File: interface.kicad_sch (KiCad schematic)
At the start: 8 parts, among them J5 Conn_01x16

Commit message: PN update
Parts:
- FB2: PN (none) -> BLM18KG601SH1D
- J5: value Conn_01x16 -> DA15_CONN; PN (none) -> TSM-108-01-L-DV-P-TR
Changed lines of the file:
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@@
       (effects (font (size 1.27 1.27)))
     )
-    (property "Value" "Conn_01x16" (at 109.22 120.1999 0)
+    (property "Value" "DA15_CONN" (at 109.22 120.1999 0)
       (effects (font (size 1.27 1.27)))
     )
@@
     )
     (property "Datasheet" "~" (at 109.22 140.97 0)
+      (effects (font (size 1.27 1.27)) hide)
+    )
+    (property "PN" "TSM-108-01-L-DV-P-TR" (at 109.22 140.97 0)
       (effects (font (size 1.27 1.27)) hide)
     )
@@
       (effects (font (size 1.27 1.27)) hide)
     )
-    (property "PN" "" (at 278.13 128.27 90)
-      (effects (font (size 1.27 1.27)) hide)
-    )
+    (property "PN" "BLM18KG601SH1D" (at 278.13 128.27 90)
+      (effects (font (size 1.27 1.27)) hide)
+    )

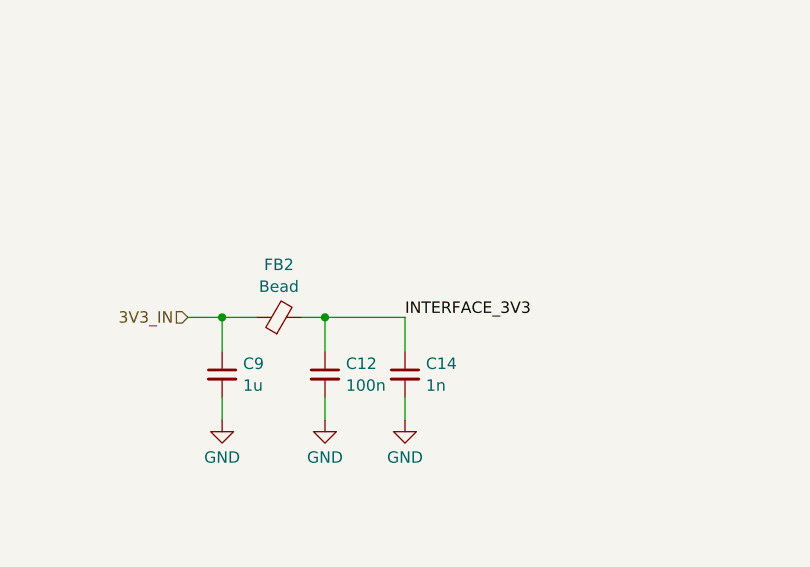
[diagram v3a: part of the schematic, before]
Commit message: `PWR_FLAG`, ERC cleanup
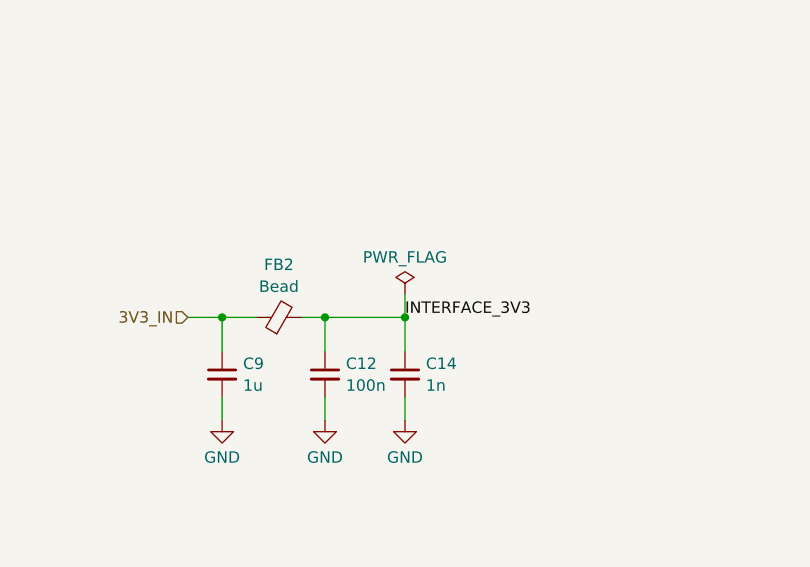
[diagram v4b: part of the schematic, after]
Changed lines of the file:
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@@
     (comment 1 "Wojciech Kaczmarski, SP5WWP")
+  )
+  (junction (at 292.1 128.27) (diameter 0) (color 0 0 0 0)
   )
   (junction (at 119.38 161.29) (diameter 0) (color 0 0 0 0)
@@
   )
   (wire (pts (xy 114.3 156.21) (xy 146.05 156.21))
+    (stroke (width 0) (type default))
+  )
+  (wire (pts (xy 292.1 125.73) (xy 292.1 128.27))
     (stroke (width 0) (type default))
   )
@@
         )
       )
+    )
+  )
+  (symbol (lib_id "power:PWR_FLAG") (at 292.1 125.73 0) (unit 1)
+    (in_bom yes) (on_board yes) (dnp no) (fields_autoplaced)
+    (property "Reference" "#FLG01" (at 292.1 123.825 0)
+      (effects (font (size 1.27 1.27)) hide)
+    )
+    (property "Value" "PWR_FLAG" (at 292.1 121.5969 0)
+      (effects (font (size 1.27 1.27)))
+    )
+    (property "Footprint" "" (at 292.1 125.73 0)
+      (effects (font (size 1.27 1.27)) hide)
+    )
+    (property "Datasheet" "~" (at 292.1 125.73 0)
+      (effects (font (size 1.27 1.27)) hide)
+    )
+    (pin "1")
+    (instances
+      (project "m17-rru-rf"
+        (path "/4c42207c-9e6b-42da-ad38-da126b892014/270fa747-1697-46c9-b996-5c9733c883e2"
+          (reference "#FLG01") (unit 1)
+        )
+        (path "/4c42207c-9e6b-42da-ad38-da126b892014/3ea647a3-6e2c-4a7a-bdb8-a6b94119ef02"
+          (reference "#FLG05") (unit 1)
+        )
+      )

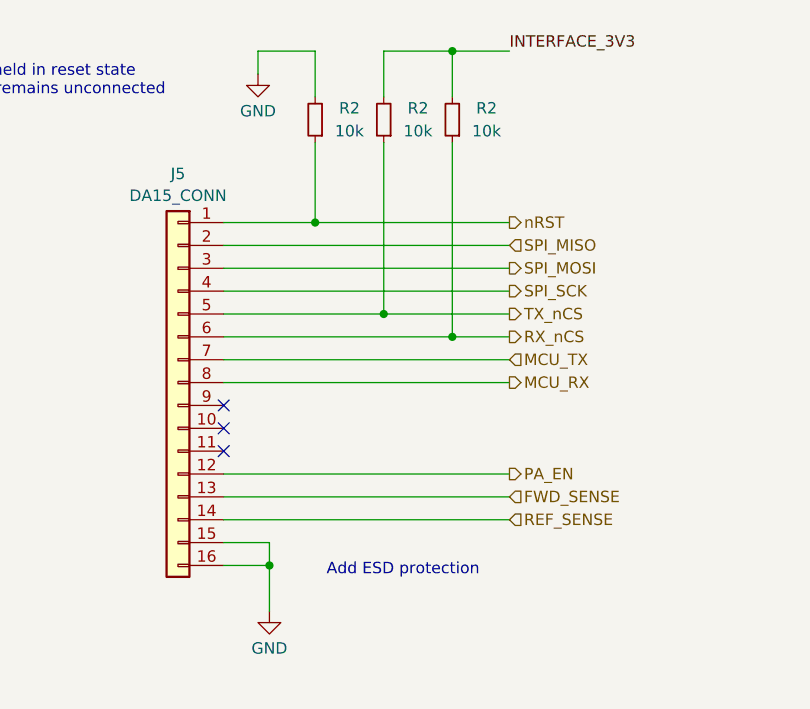
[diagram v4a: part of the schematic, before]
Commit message: TP updates, temp sensor added
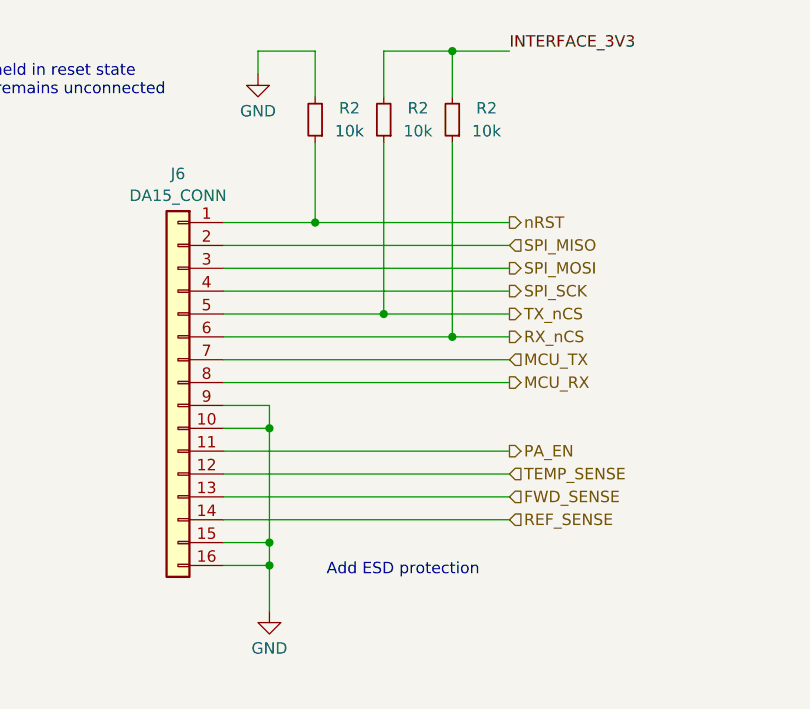
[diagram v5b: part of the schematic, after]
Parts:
- renumbered J5 to J6
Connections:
- net GND: now also J6.10 (Pin_10), J6.9 (Pin_9)
- net PA_EN: now also J6.11 (Pin_11); no longer J6.12 (Pin_12)
- new net TEMP_SENSE: J6.12 (Pin_12)
- no-connect marks 3 -> 0
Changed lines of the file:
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@@
     (comment 1 "Wojciech Kaczmarski, SP5WWP")
   )
+  (junction (at 119.38 158.75) (diameter 0) (color 0 0 0 0)
+  )
   (junction (at 292.1 128.27) (diameter 0) (color 0 0 0 0)
   )
@@
   (junction (at 139.7 135.89) (diameter 0) (color 0 0 0 0)
   )
+  (junction (at 119.38 146.05) (diameter 0) (color 0 0 0 0)
+  )
   (junction (at 283.21 128.27) (diameter 0) (color 0 0 0 0)
   )
@@
   (junction (at 271.78 128.27) (diameter 0) (color 0 0 0 0)
   )
-  (no_connect (at 114.3 143.51))
-  (no_connect (at 114.3 146.05))
-  (no_connect (at 114.3 148.59))
   (wire (pts (xy 124.46 114.3) (xy 124.46 123.19))
     (stroke (width 0) (type default))
   )
+  (wire (pts (xy 114.3 148.59) (xy 146.05 148.59))
+    (stroke (width 0) (type default))
+  )
+  (wire (pts (xy 114.3 125.73) (xy 146.05 125.73))
+    (stroke (width 0) (type default))
+  )
+  (wire (pts (xy 118.11 106.68) (xy 118.11 104.14))
+    (stroke (width 0) (type default))
+  )
+  (wire (pts (xy 132.08 133.35) (xy 146.05 133.35))
+    (stroke (width 0) (type default))
+  )
+  (wire (pts (xy 283.21 137.16) (xy 283.21 139.7))
+    (stroke (width 0) (type default))
+  )
+  (wire (pts (xy 119.38 158.75) (xy 119.38 161.29))
+    (stroke (width 0) (type default))
+  )
+  (wire (pts (xy 292.1 137.16) (xy 292.1 139.7))
+    (stroke (width 0) (type default))
+  )
+  (wire (pts (xy 292.1 132.08) (xy 292.1 128.27))
+    (stroke (width 0) (type default))
+  )
+  (wire (pts (xy 132.08 114.3) (xy 132.08 133.35))
+    (stroke (width 0) (type default))
+  )
   (wire (pts (xy 114.3 151.13) (xy 146.05 151.13))
     (stroke (width 0) (type default))
   )
-  (wire (pts (xy 114.3 125.73) (xy 146.05 125.73))
-    (stroke (width 0) (type default))
-  )
-  (wire (pts (xy 118.11 106.68) (xy 118.11 104.14))
-    (stroke (width 0) (type default))
-  )
-  (wire (pts (xy 132.08 133.35) (xy 146.05 133.35))
-    (stroke (width 0) (type default))
-  )
-  (wire (pts (xy 283.21 137.16) (xy 283.21 139.7))
-    (stroke (width 0) (type default))
-  )
-  (wire (pts (xy 119.38 158.75) (xy 119.38 161.29))
-    (stroke (width 0) (type default))
-  )
-  (wire (pts (xy 292.1 137.16) (xy 292.1 139.7))
-    (stroke (width 0) (type default))
-  )
-  (wire (pts (xy 292.1 132.08) (xy 292.1 128.27))
-    (stroke (width 0) (type default))
-  )
-  (wire (pts (xy 132.08 114.3) (xy 132.08 133.35))
-    (stroke (width 0) (type default))
-  )
   (wire (pts (xy 114.3 156.21) (xy 146.05 156.21))
     (stroke (width 0) (type default))
@@
     (stroke (width 0) (type default))
   )
+  (wire (pts (xy 114.3 146.05) (xy 119.38 146.05))
+    (stroke (width 0) (type default))
+  )
   (wire (pts (xy 119.38 161.29) (xy 119.38 166.37))
     (stroke (width 0) (type default))
@@
     (stroke (width 0) (type default))
   )
+  (wire (pts (xy 114.3 143.51) (xy 119.38 143.51))
+    (stroke (width 0) (type default))
+  )
   (wire (pts (xy 132.08 104.14) (xy 139.7 104.14))
     (stroke (width 0) (type default))
   )
+  (wire (pts (xy 119.38 143.51) (xy 119.38 146.05))
+    (stroke (width 0) (type default))
+  )
   (wire (pts (xy 132.08 109.22) (xy 132.08 104.14))
     (stroke (width 0) (type default))
@@
   )
   (wire (pts (xy 139.7 135.89) (xy 146.05 135.89))
+    (stroke (width 0) (type default))
+  )
+  (wire (pts (xy 119.38 146.05) (xy 119.38 158.75))
     (stroke (width 0) (type default))
   )
@@
     (effects (font (size 1.27 1.27)) (justify left bottom))
   )
+  (hierarchical_label "TEMP_SENSE" (shape input) (at 146.05 151.13 0) (fields_autoplaced)
+    (effects (font (size 1.27 1.27)) (justify left))
+  )
   (hierarchical_label "FWD_SENSE" (shape input) (at 146.05 153.67 0) (fields_autoplaced)
     (effects (font (size 1.27 1.27)) (justify left))
@@
     (effects (font (size 1.27 1.27)) (justify left))
   )
-  (hierarchical_label "PA_EN" (shape output) (at 146.05 151.13 0) (fields_autoplaced)
+  (hierarchical_label "PA_EN" (shape output) (at 146.05 148.59 0) (fields_autoplaced)
     (effects (font (size 1.27 1.27)) (justify left))
   )
@@
   (symbol (lib_id "Connector_Generic:Conn_01x16") (at 109.22 140.97 0) (mirror y) (unit 1)
     (in_bom yes) (on_board yes) (dnp no) (fields_autoplaced)
-    (property "Reference" "J5" (at 109.22 117.7757 0)
+    (property "Reference" "J6" (at 109.22 117.7757 0)
       (effects (font (size 1.27 1.27)))
     )
@@
       (project "m17-rru-rf"
         (path "/4c42207c-9e6b-42da-ad38-da126b892014/3ea647a3-6e2c-4a7a-bdb8-a6b94119ef02"
-          (reference "J5") (unit 1)
+          (reference "J6") (unit 1)
         )
       )
@@
         )
         (path "/4c42207c-9e6b-42da-ad38-da126b892014/3ea647a3-6e2c-4a7a-bdb8-a6b94119ef02"
-          (reference "#PWR0110") (unit 1)
+          (reference "#PWR0115") (unit 1)
         )
       )
@@
         )
         (path "/4c42207c-9e6b-42da-ad38-da126b892014/3ea647a3-6e2c-4a7a-bdb8-a6b94119ef02"
-          (reference "#PWR0112") (unit 1)
+          (reference "#PWR0117") (unit 1)
         )
       )
@@
         )
         (path "/4c42207c-9e6b-42da-ad38-da126b892014/3ea647a3-6e2c-4a7a-bdb8-a6b94119ef02"
-          (reference "#PWR0111") (unit 1)
+          (reference "#PWR0116") (unit 1)
         )
       )
@@
         )
         (path "/4c42207c-9e6b-42da-ad38-da126b892014/3ea647a3-6e2c-4a7a-bdb8-a6b94119ef02"
-          (reference "C89") (unit 1)
+          (reference "C92") (unit 1)
         )
       )
@@
         )
         (path "/4c42207c-9e6b-42da-ad38-da126b892014/3ea647a3-6e2c-4a7a-bdb8-a6b94119ef02"
-          (reference "C87") (unit 1)
+          (reference "C90") (unit 1)
         )
       )
@@
         )
         (path "/4c42207c-9e6b-42da-ad38-da126b892014/3ea647a3-6e2c-4a7a-bdb8-a6b94119ef02"
-          (reference "FB7") (unit 1)
+          (reference "FB9") (unit 1)
         )
       )
@@
         )
         (path "/4c42207c-9e6b-42da-ad38-da126b892014/3ea647a3-6e2c-4a7a-bdb8-a6b94119ef02"
-          (reference "C88") (unit 1)
+          (reference "C91") (unit 1)
         )
       )
@@
         )
         (path "/4c42207c-9e6b-42da-ad38-da126b892014/3ea647a3-6e2c-4a7a-bdb8-a6b94119ef02"
-          (reference "#PWR0114") (unit 1)
+          (reference "#PWR0119") (unit 1)
         )
       )
@@
         )
         (path "/4c42207c-9e6b-42da-ad38-da126b892014/3ea647a3-6e2c-4a7a-bdb8-a6b94119ef02"
-          (reference "#FLG05") (unit 1)
+          (reference "#FLG08") (unit 1)
         )
       )
@@
         )
         (path "/4c42207c-9e6b-42da-ad38-da126b892014/3ea647a3-6e2c-4a7a-bdb8-a6b94119ef02"
-          (reference "#PWR0113") (unit 1)
-        )
-      )
+          (reference "#PWR0118") (unit 1)
+        )
+      )

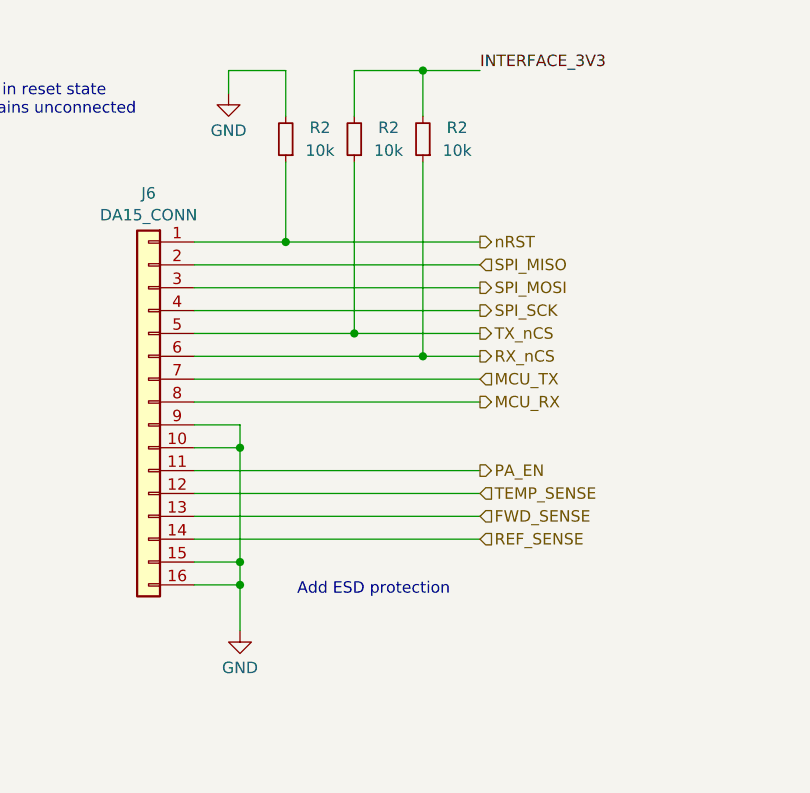
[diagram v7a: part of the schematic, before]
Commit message: `DA15_CONN` pinout change
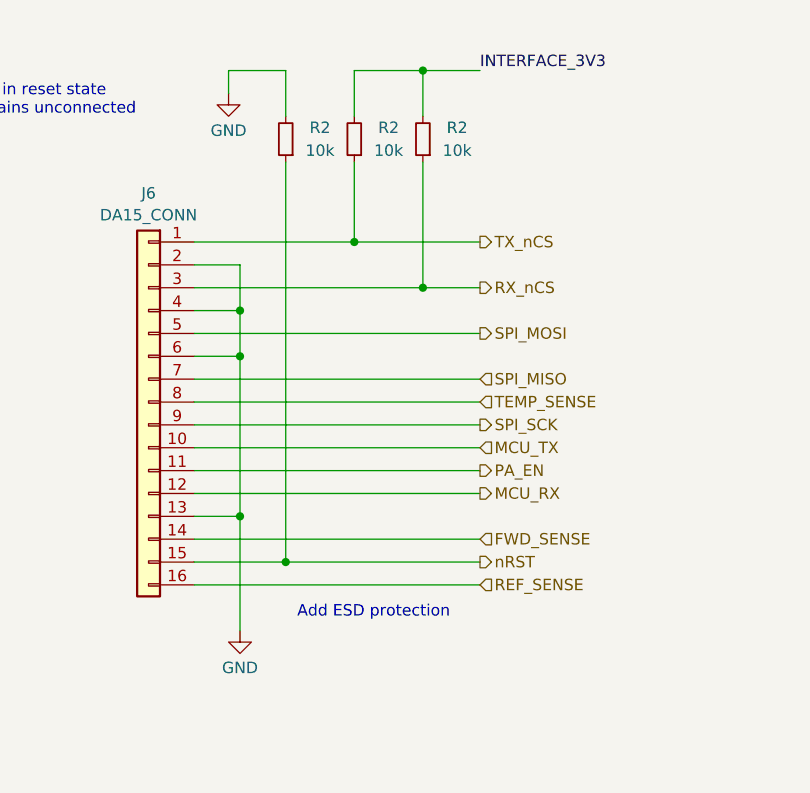
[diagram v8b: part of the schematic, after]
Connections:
- net FWD_SENSE: now also J6.14 (Pin_14); no longer J6.13 (Pin_13)
- net GND: now also J6.13 (Pin_13), J6.2 (Pin_2), J6.4 (Pin_4), J6.6 (Pin_6); no longer J6.10 (Pin_10), J6.15 (Pin_15), J6.16 (Pin_16), J6.9 (Pin_9)
- net MCU_RX: now also J6.12 (Pin_12); no longer J6.8 (Pin_8)
- net MCU_TX: now also J6.10 (Pin_10); no longer J6.7 (Pin_7)
- net REF_SENSE: now also J6.16 (Pin_16); no longer J6.14 (Pin_14)
- net RX_nCS: now also J6.3 (Pin_3); no longer J6.6 (Pin_6)
- net SPI_MISO: now also J6.7 (Pin_7); no longer J6.2 (Pin_2)
- net SPI_MOSI: now also J6.5 (Pin_5); no longer J6.3 (Pin_3)
- net SPI_SCK: now also J6.9 (Pin_9); no longer J6.4 (Pin_4)
- net TEMP_SENSE: now also J6.8 (Pin_8); no longer J6.12 (Pin_12)
- net TX_nCS: now also J6.1 (Pin_1); no longer J6.5 (Pin_5)
- net nRST: now also J6.15 (Pin_15); no longer J6.1 (Pin_1)
